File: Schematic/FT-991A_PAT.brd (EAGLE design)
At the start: 44.6 x 59.8 mm, 31 parts, among them Q1 PE4259, Q2 MC78L09ABDR2GOSCT, Q5 NCP553, Q7 J310, Q8 BFR193F, X1 IF_IN, X2 SCP_OUT, X3 SDR_OUT

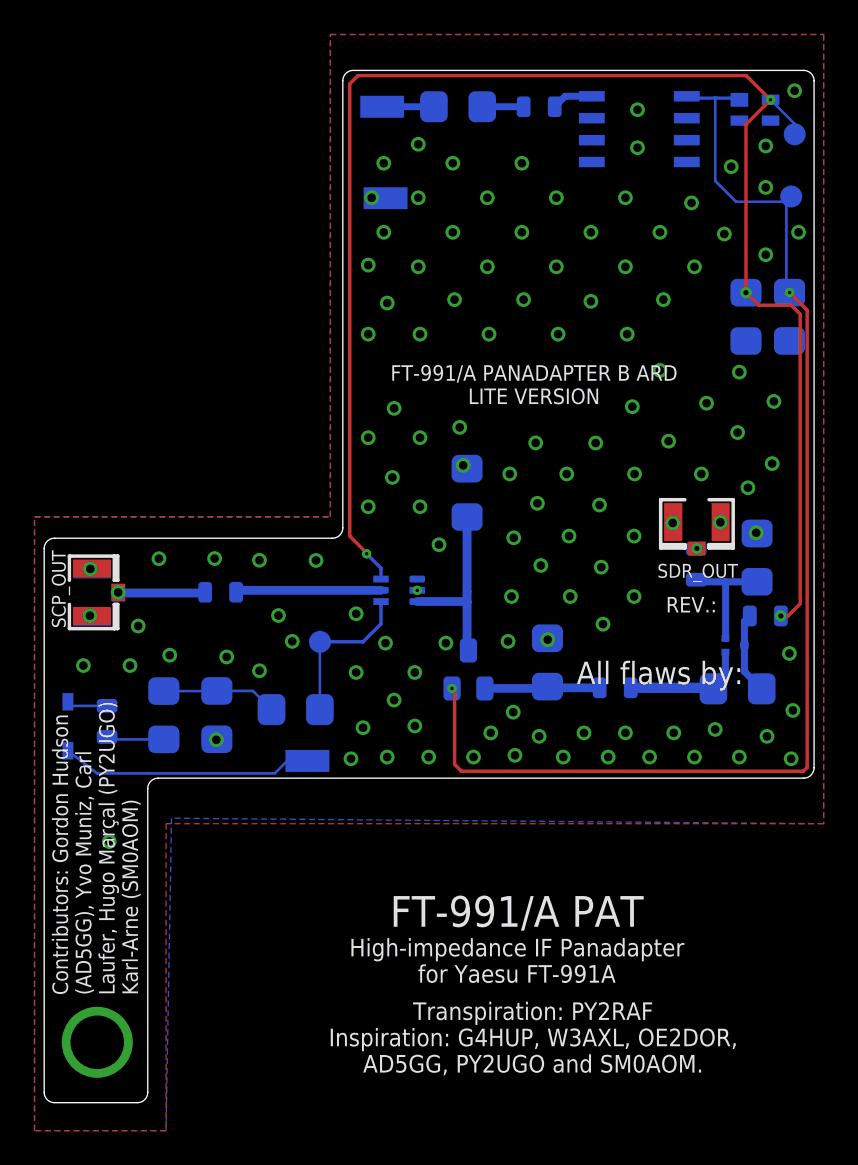
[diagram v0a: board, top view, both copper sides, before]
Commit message: Rev. S: New RF switch actuation
* New RF switch design - now uses an analog switch to flip the RF switch.
  While this added new parts (1 switch and two resistors) and extra
  complexity, this actuation format is industry-standard and allows
  for substitutes of PE4259 (which is unobtanium as of now).

* New component in library (NLAS4599)
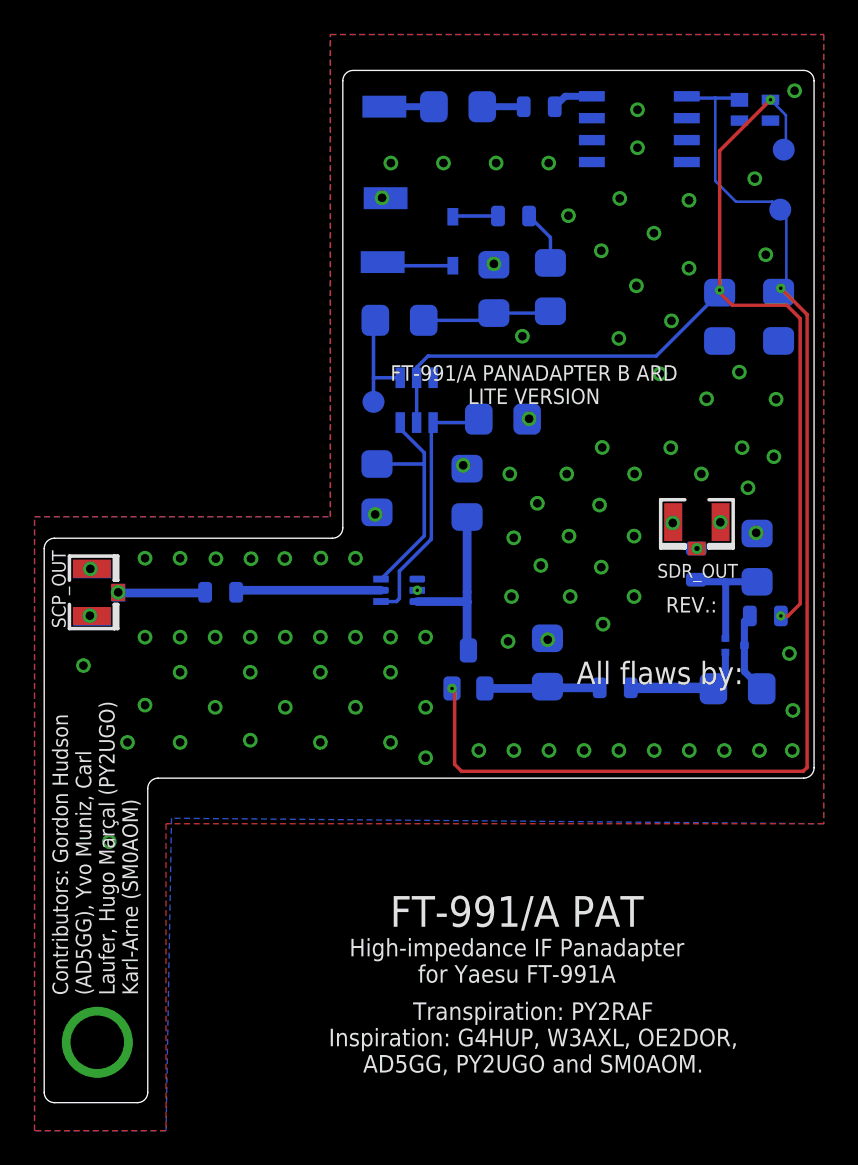
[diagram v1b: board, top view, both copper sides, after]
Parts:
- added Q3: NLAS4599, aarf:SOT23-6
- added R1, R6: 100kΩ, aarf:1206
- moved L3 37.6 mm to (33.5, 63.0), turned to 180 degrees
- moved D1 35.9 mm to (30.0, 61.6)
- moved R3 33.4 mm to (35.6, 58.9), turned to 90 degrees
- moved R4 29.4 mm to (32.4, 58.7), turned to 90 degrees
- moved PAD3 29.2 mm to (25.9, 60.3), turned to 90 degrees
- moved R2 23.3 mm to (26.9, 56.9), turned to 0 degrees
- moved TP3 14.2 mm to (25.4, 52.2)
- moved C11 1.52 mm to (45.5, 57.1)
- moved TP2 1.09 mm to (49.2, 66.8)
- moved TP1 0.99 mm to (49.0, 63.3)
- moved C7 0.63 mm to (48.9, 57.1)
- moved 13.8V 0.13 mm to (26.0, 69.3)
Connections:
- new net N$2: Q1.4, Q3.4, R6.2
- new net N$6: Q1.6, Q3.6, R1.2
- net 3V: now also Q3.2, Q3.5; no longer Q1.6
- net GNDA: now also Q3.3, R1.1, R6.1
- net N$7: now also Q3.1; no longer Q1.4
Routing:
- net 3V: track 90.6 -> 61.6 mm, vias 4 -> 3
- net N$2: track 0.00 -> 14.9 mm
- net N$6: track 0.00 -> 13.4 mm
- net N$18: track 14.6 -> 4.15 mm
- net N$7: track 9.15 -> 6.46 mm
- net N$8: track 6.87 -> 8.56 mm
- net 9V: track 72.1 -> 71.4 mm

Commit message: Minor board fixes
* Ran board through DRC and added some extra clearances
* Analog switch label silkscreen was missing
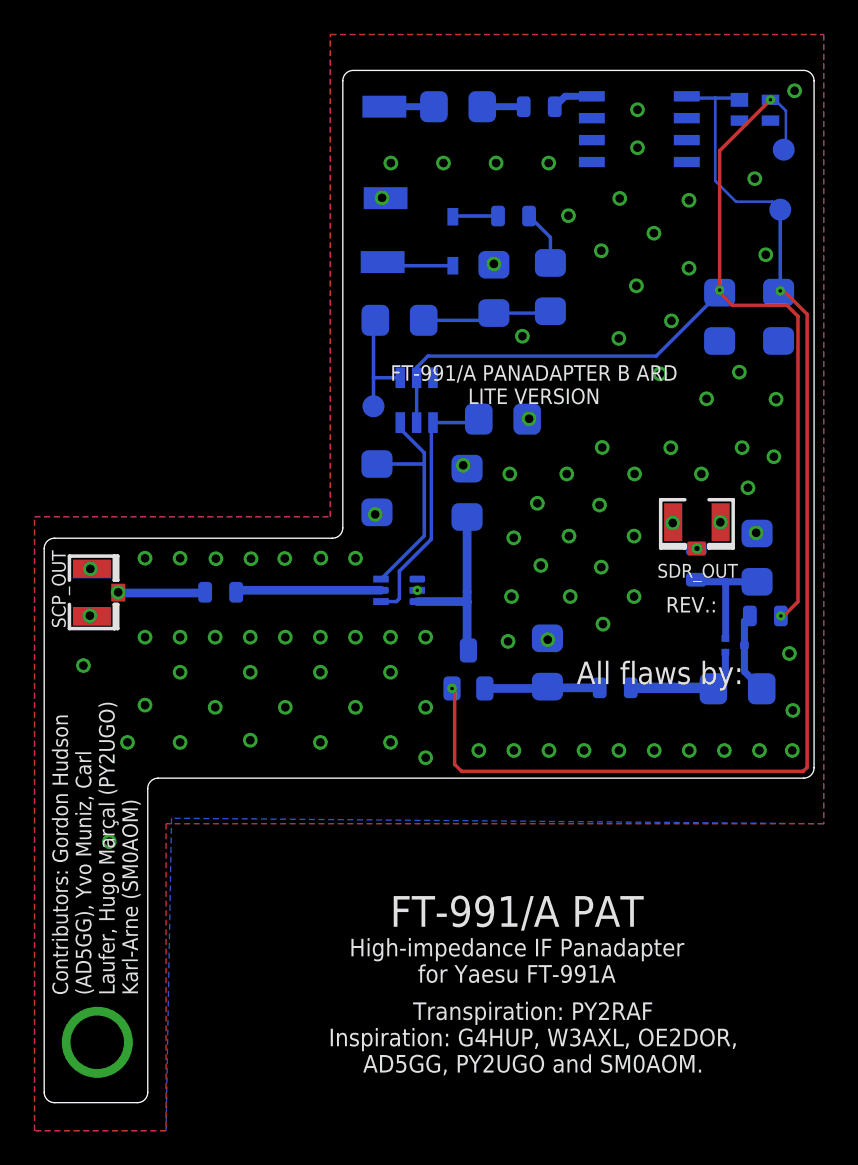
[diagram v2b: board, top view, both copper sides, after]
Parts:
- moved TP3 0.25 mm to (25.4, 51.9)
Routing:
- net N$8: track 8.56 -> 7.69 mm
- net 9V: track 71.4 -> 70.7 mm
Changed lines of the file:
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@@
 <drawing>
 <settings>
-<setting alwaysvectorfont="yes"/>
+<setting alwaysvectorfont="no"/>
 <setting keepoldvectorfont="yes"/>
 <setting verticaltext="up"/>
 </settings>
-<grid distance="5" unitdist="mil" unit="mil" style="lines" multiple="8" display="yes" altdistance="100" altunitdist="mil" altunit="mil"/>
+<grid distance="5" unitdist="mil" unit="mil" style="lines" multiple="8" display="no" altdistance="100" altunitdist="mil" altunit="mil"/>
 <layers>
 <layer number="1" name="Top" color="4" fill="1" visible="yes" active="yes"/>
@@
 <attribute name="VALUE" x="49.8" y="66.049" size="0.0254" layer="28" rot="MR0"/>
 </element>
-<element name="TP3" library="testpad" library_urn="urn:adsk.eagle:library:385" package="B1,27" package3d_urn="urn:adsk.eagle:package:27944/1" value="3V" x="25.4" y="52.2" smashed="yes" rot="MR0">
-<attribute name="TP_SIGNAL_NAME" value="" x="25.4" y="52.2" size="1.778" layer="28" rot="MR0" display="off"/>
-<attribute name="VALUE" x="26.035" y="51.438" size="0.0254" layer="28" rot="MR0"/>
+<element name="TP3" library="testpad" library_urn="urn:adsk.eagle:library:385" package="B1,27" package3d_urn="urn:adsk.eagle:package:27944/1" value="3V" x="25.4" y="51.946" smashed="yes" rot="MR0">
+<attribute name="TP_SIGNAL_NAME" value="" x="25.4" y="51.946" size="1.778" layer="28" rot="MR0" display="off"/>
 </element>
 <element name="Q7" library="aarf" package="SOT23-3" value="J310" x="30.9" y="36.7" smashed="yes" rot="MR0">
@@
 </element>
 <element name="Q3" library="aarf" package="SOT23-6" value="NLAS4599" x="27.9" y="52.3" smashed="yes" rot="MR180">
-<attribute name="VALUE" x="25.995" y="55.729" size="1.27" layer="28" rot="MR180"/>
+<attribute name="VALUE" x="29.996" y="52.538" size="0.7874" layer="22" font="vector" ratio="15" rot="MR90" align="center"/>
 </element>
 <element name="R1" library="aarf" package="1206" value="100kΩ" x="25.6" y="47.2" smashed="yes" rot="MR90">
@@
 <contactref element="X2" pad="3"/>
 <via x="10.60911875" y="41.166790625" extent="1-16" drill="0.5"/>
-<wire x1="15.645478125" y1="41.1711" x2="15.410509375" y2="41.12915625" width="0.508" layer="16"/>
-<wire x1="10.628890625" y1="41.12915625" x2="15.410509375" y2="41.12915625" width="0.508" layer="16"/>
+<wire x1="10.628890625" y1="41.12915625" x2="15.603534375" y2="41.12915625" width="0.508" layer="16"/>
+<wire x1="15.603534375" y1="41.12915625" x2="15.645478125" y2="41.1711" width="0.508" layer="16"/>
 <wire x1="10.628890625" y1="41.12915625" x2="10.60911875" y2="41.166790625" width="0" layer="19" extent="1-16"/>
 </signal>
@@
 <contactref element="R4" pad="1"/>
 <contactref element="R2" pad="1"/>
-<wire x1="31.75378125" y1="56.72544375" x2="32.373678125" y2="57.345340625" width="0.2032" layer="16"/>
 <wire x1="32.373678125" y1="57.345340625" x2="32.5" y2="57.345340625" width="0.2032" layer="16"/>
 <wire x1="32.5" y1="57.345340625" x2="35.5422" y2="57.345340625" width="0.2032" layer="16"/>
@@
 <wire x1="30.8225" y1="40.6" x2="30.8225" y2="37.8775" width="0.508" layer="16"/>
 <wire x1="30.9" y1="37.8" x2="30.8225" y2="37.8775" width="0.4064" layer="16"/>
-<wire x1="30.8225" y1="41.190896875" x2="30.7725" y2="41.240896875" width="0.4064" layer="16"/>
 <wire x1="27.935" y1="40.635" x2="30.7875" y2="40.635" width="0.508" layer="16"/>
 <wire x1="30.7875" y1="40.635" x2="30.8225" y2="40.6" width="0.508" layer="16"/>
@@
 <contactref element="R2" pad="2"/>
 <contactref element="TP3" pad="TP"/>
-<wire x1="25.4" y1="52.2" x2="25.335" y2="52.265" width="0.2" layer="16"/>
-<wire x1="25.39288125" y1="52.19288125" x2="25.4" y2="52.2" width="0.15" layer="16"/>
 <contactref element="Q3" pad="1"/>
 <wire x1="25.55" y1="56.8825625" x2="25.50711875" y2="56.92544375" width="0.2032" layer="16"/>
-<wire x1="25.4" y1="52.2" x2="25.4" y2="53.6" width="0.2032" layer="16"/>
 <wire x1="25.4" y1="53.6" x2="25.4" y2="56.7325625" width="0.2032" layer="16"/>
 <wire x1="25.4" y1="56.7325625" x2="25.55" y2="56.8825625" width="0.2032" layer="16"/>
 <wire x1="26.95" y1="53.6" x2="25.4" y2="53.6" width="0.2032" layer="16"/>
+<wire x1="25.4" y1="51.946" x2="25.39288125" y2="51.93888125" width="0.2032" layer="16"/>
+<wire x1="25.4" y1="51.946" x2="25.4" y2="53.6" width="0.2032" layer="16"/>
 </signal>
 <signal name="9V">
@@
 <contactref element="Q2" pad="1"/>
 <contactref element="TP1" pad="TP"/>
-<via x="48.9945" y="58.7865" extent="1-16" drill="0.2"/>
-<wire x1="48.9945" y1="58.7865" x2="50.5225" y2="57.2585" width="0.2" layer="1"/>
 <wire x1="50.5225" y1="31.025" x2="50.3" y2="30.8025" width="0.2" layer="1"/>
-<wire x1="50.5225" y1="57.2585" x2="50.5225" y2="31.025" width="0.2" layer="1"/>
+<wire x1="50.5225" y1="57.277" x2="50.5225" y2="31.025" width="0.2" layer="1"/>
 <wire x1="30.4975" y1="30.8025" x2="50.3" y2="30.8025" width="0.2" layer="1"/>
 <wire x1="30.4975" y1="30.8025" x2="30.1" y2="31.2" width="0.2" layer="1"/>
@@
 <wire x1="43.655" y1="69.8" x2="43.55" y2="69.905" width="0.2" layer="16"/>
 <wire x1="46.5" y1="69.8" x2="46.6" y2="69.7" width="0.2" layer="16"/>
-<wire x1="48.965" y1="58.63" x2="48.8675" y2="58.5325" width="0.1524" layer="16"/>
-<wire x1="48.765" y1="63.338" x2="48.965" y2="63.338" width="0.1524" layer="16"/>
-<wire x1="49.3178" y1="62.9852" x2="49.3178" y2="58.9828" width="0.1524" layer="16"/>
-<wire x1="48.8675" y1="58.5325" x2="49.3178" y2="58.9828" width="0.1524" layer="16"/>
-<wire x1="49.3178" y1="62.9852" x2="48.965" y2="63.338" width="0.1524" layer="16"/>
 <wire x1="48.965" y1="63.338" x2="48.503" y2="63.8" width="0.1524" layer="16"/>
 <wire x1="46.4" y1="63.8" x2="45.2" y2="65" width="0.1524" layer="16"/>
 <wire x1="48.503" y1="63.8" x2="46.4" y2="63.8" width="0.1524" layer="16"/>
 <wire x1="45.2" y1="65" x2="45.2" y2="69.8" width="0.1524" layer="16"/>
-<wire x1="48.9945" y1="58.7865" x2="48.965" y2="58.63" width="0" layer="19" extent="16-16"/>
+<wire x1="48.965" y1="63.338" x2="48.965" y2="58.63" width="0.2032" layer="16"/>
+<wire x1="48.8675" y1="58.5325" x2="48.965" y2="58.63" width="0.2032" layer="16"/>
+<via x="48.965" y="58.63" extent="1-16" drill="0.2"/>
+<wire x1="50.5225" y1="57.277" x2="49.1695" y2="58.63" width="0.2032" layer="1"/>
+<wire x1="49.1695" y1="58.63" x2="48.965" y2="58.63" width="0.2032" layer="1"/>
 </signal>
 <signal name="3V">
@@
 <contactref element="TP2" pad="TP"/>
 <via x="48.4" y="69.7" extent="1-16" drill="0.2"/>
-<wire x1="49.292" y1="68.808" x2="49.292" y2="66.938" width="0.1524" layer="16"/>
+<wire x1="49.292" y1="69.062" x2="49.292" y2="66.938" width="0.1524" layer="16"/>
 <wire x1="49.165" y1="66.811" x2="49.292" y2="66.938" width="0.1524" layer="16"/>
-<wire x1="49.292" y1="68.808" x2="48.4" y2="69.7" width="0.1524" layer="16"/>
+<wire x1="49.292" y1="69.062" x2="48.654" y2="69.7" width="0.1524" layer="16"/>
+<wire x1="48.654" y1="69.7" x2="48.4" y2="69.7" width="0.1524" layer="16"/>
 <wire x1="45.4535" y1="58.5275" x2="46.181" y2="57.8" width="0.2" layer="1"/>
 <wire x1="46.181" y1="57.8" x2="49.346" y2="57.8" width="0.2" layer="1"/>
-<wire x1="49.346" y1="57.8" x2="50.1193" y2="57.0267" width="0.2" layer="1"/>
-<wire x1="50.1193" y1="57.0267" x2="50.1193" y2="40.5" width="0.2" layer="1"/>
+<wire x1="49.346" y1="57.8" x2="49.9923" y2="57.1537" width="0.2" layer="1"/>
+<wire x1="49.9923" y1="57.1537" x2="49.9923" y2="40.627" width="0.2" layer="1"/>
 <wire x1="45.4535" y1="58.5275" x2="45.4535" y2="58.674" width="0.2" layer="1"/>
 <wire x1="45.4535" y1="58.674" x2="45.4535" y2="66.7535" width="0.2" layer="1"/>
 <wire x1="45.4535" y1="66.7535" x2="48.4" y2="69.7" width="0.2" layer="1"/>
 <contactref element="L1" pad="P$1"/>
-<wire x1="50.1193" y1="40.5" x2="49.419284375" y2="39.799984375" width="0.2032" layer="1"/>
-<wire x1="49.419284375" y1="39.799984375" x2="49" y2="39.8" width="0.2032" layer="1"/>
+<wire x1="49.9923" y1="40.627" x2="49.16529375" y2="39.79999375" width="0.2032" layer="1"/>
+<wire x1="49.16529375" y1="39.79999375" x2="49" y2="39.8" width="0.2032" layer="1"/>
 <contactref element="C11" pad="1"/>
 <contactref element="Q3" pad="2"/>
@@
 <contactref element="Q8" pad="3"/>
 <contactref element="L1" pad="P$2"/>
-<wire x1="47.8875" y1="35.5825" x2="47.8925" y2="35.5775" width="0.6096" layer="16"/>
 <wire x1="47.8925" y1="35.5775" x2="46.8875" y2="36.5825" width="0.4064" layer="16"/>
 <wire x1="46.8875" y1="36.5825" x2="46.8875" y2="38.0975" width="0.4064" layer="16"/>
